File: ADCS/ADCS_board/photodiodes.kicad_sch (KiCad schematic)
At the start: 6 parts, among them J1 5055680431, J10 5055680631, J3 5055680431, J4 5055680631, J6 5055680431, J9 5055680431

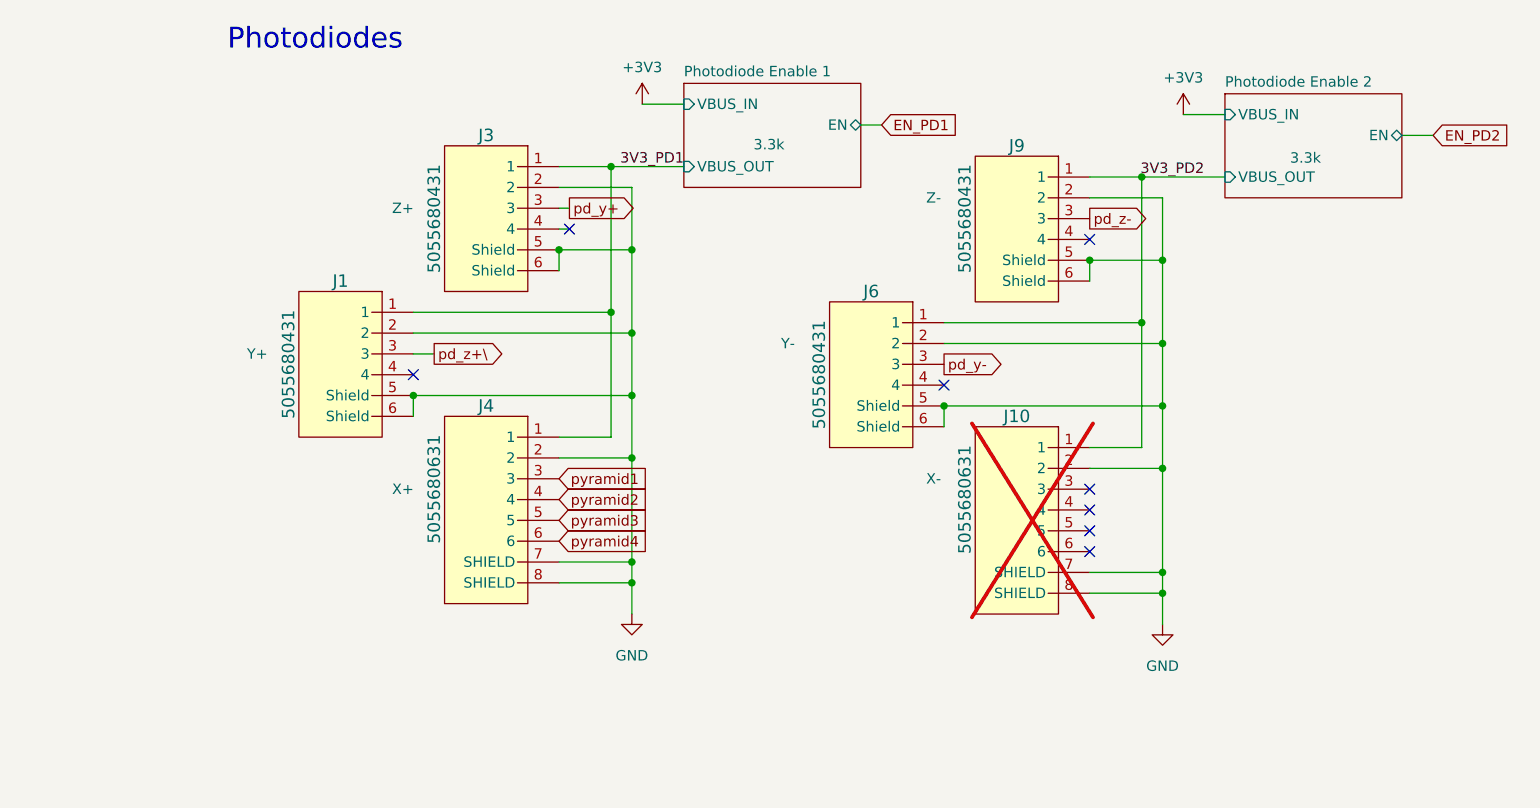
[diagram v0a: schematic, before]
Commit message: main adcs board with initial traces coming out of MCU
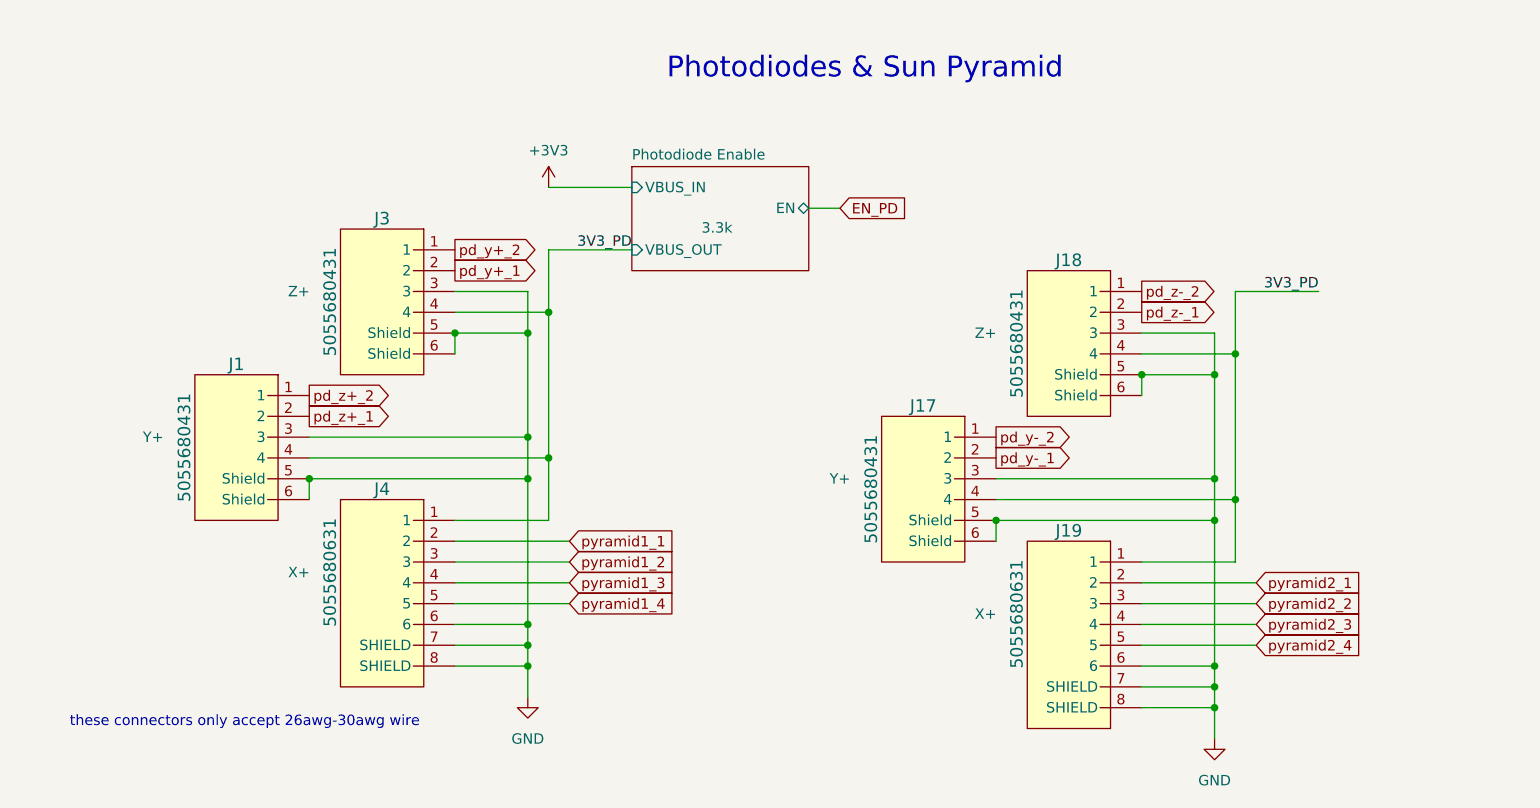
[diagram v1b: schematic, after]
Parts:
- removed J10: 5055680631, adcs:CON_5055680631, symbol adcs:5055680631
- removed J6, J9: 5055680431, adcs:CON_5055680431, symbol adcs:5055680431
- added J17, J18: 5055680431, adcs:CON_5055680431, symbol adcs:5055680431
- added J19: 5055680631, adcs:CON_5055680631, symbol adcs:5055680631
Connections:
- net pd_y+ is gone; now on net GND: J3.3
- net pd_z+\ is gone; now on net GND: J1.3
- net pyramid4 is gone; now on net GND: J4.6
- net GND: now also J17.3, J17.5 (Shield), J17.6 (Shield), J18.3, J18.5 (Shield), J18.6 (Shield), J19.6, J19.7 (SHIELD), J19.8 (SHIELD); no longer J1.2, J3.2, J4.2
- net 3V3_PD: now reaches J3.4
- net 3V3_PD: now also J1.4, J4.1, J17.4, J18.4, J19.1
- removed net 3V3_PD1: J1.1, J3.1, J4.1
- net pyramid1 renamed pyramid1_2
- net pyramid2 renamed pyramid1_3
- net pyramid3 renamed pyramid1_4
- new net pd_y+_1: J3.2
- new net pd_y+_2: J3.1
- new net pd_y-_1: J17.2
- new net pd_y-_2: J17.1
- new net pd_z+_1: J1.2
- new net pd_z+_2: J1.1
- new net pd_z-_1: J18.2
- new net pd_z-_2: J18.1
- new net pyramid1_1: J4.2
- new net pyramid2_1: J19.2
- new net pyramid2_2: J19.3
- new net pyramid2_3: J19.4
- new net pyramid2_4: J19.5
- no-connect marks 8 -> 0
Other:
- sheet Photodiode Enable 1 renamed Photodiode Enable
- removed sheet Photodiode Enable 2
- note added: "Photodiodes & Sun Pyramid"
- note added: "these connectors only accept 26awg-30awg wire"
- note removed: "Photodiodes"
